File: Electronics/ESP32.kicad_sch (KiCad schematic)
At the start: 13 parts, among them Q10 RSC002P03, Q7 BSH108, Q8 BSH108, Q9 BSH108, U9 ESP32-WROOM-32D

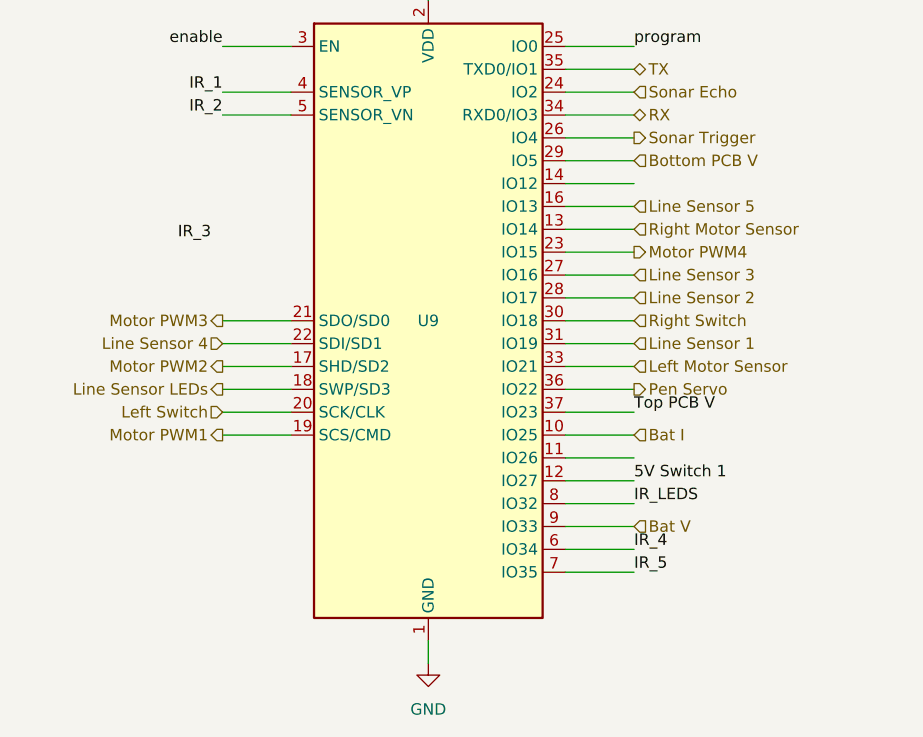
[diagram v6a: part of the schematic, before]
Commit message: Fixed the enable pin being used
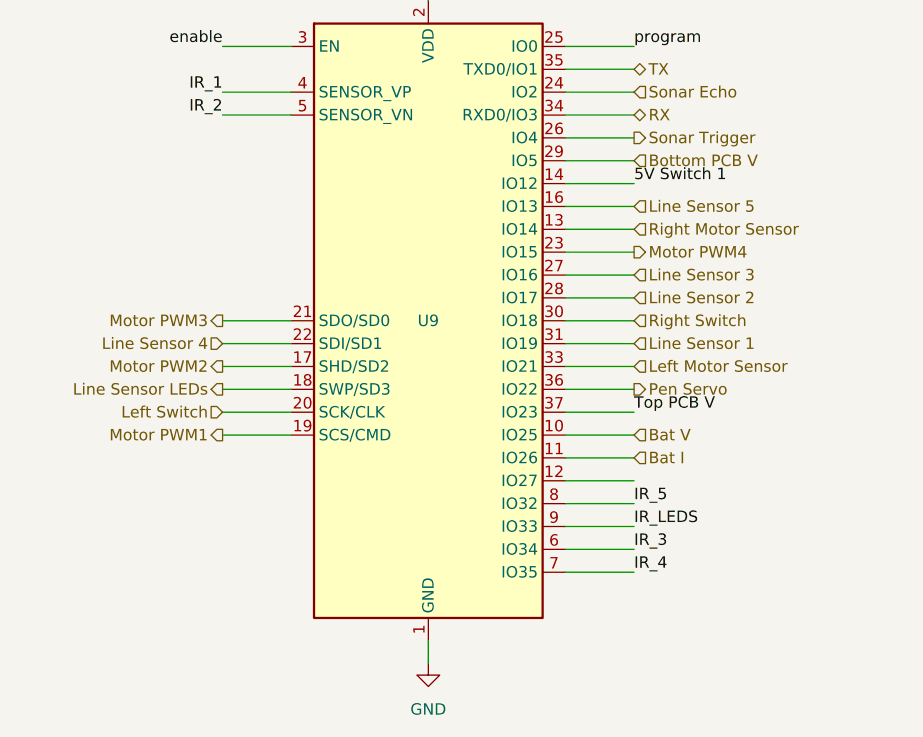
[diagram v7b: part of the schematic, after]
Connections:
- net 5V Switch 1: now also U9.14 (IO12); no longer U9.12 (IO27)
- net Bat I: now also U9.11 (IO26); no longer U9.10 (IO25)
- net Bat V: now also U9.10 (IO25); no longer U9.9 (IO33)
- net IR_3: now also U9.6 (IO34)
- net IR_4: now also U9.7 (IO35); no longer U9.6 (IO34)
- net IR_5: now also U9.8 (IO32); no longer U9.7 (IO35)
- net IR_LEDS: now also U9.9 (IO33); no longer U9.8 (IO32)
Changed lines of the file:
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@@
     (comment 1 "Design by Philip McGaw")
   )
-  (junction (at 64.77 121.92) (diameter 0) (color 0 0 0 0))
+  (junction (at 64.77 44.45) (diameter 0) (color 0 0 0 0))
   (junction (at 81.28 130.81) (diameter 0) (color 0 0 0 0))
   (junction (at 64.77 82.55) (diameter 0) (color 0 0 0 0))
   (junction (at 57.15 129.54) (diameter 0) (color 0 0 0 0))
   (junction (at 64.77 111.76) (diameter 0) (color 0 0 0 0))
-  (junction (at 64.77 44.45) (diameter 0) (color 0 0 0 0))
+  (junction (at 64.77 121.92) (diameter 0) (color 0 0 0 0))
   (wire (pts (xy 235.585 90.17) (xy 245.745 90.17))
     (stroke (width 0) (type default) (color 0 0 0 0))
@@
     (effects (font (size 1.27 1.27)) (justify left bottom))
   )
-  (label "IR_5" (at 182.88 102.87 0)
+  (label "IR_5" (at 182.88 95.25 0)
     (effects (font (size 1.27 1.27)) (justify left bottom))
   )
@@
     (effects (font (size 1.27 1.27)) (justify right bottom))
   )
-  (label "IR_4" (at 182.88 100.33 0)
+  (label "IR_4" (at 182.88 102.87 0)
     (effects (font (size 1.27 1.27)) (justify left bottom))
   )
@@
     (effects (font (size 1.27 1.27)) (justify right bottom))
   )
-  (label "5V Switch 1" (at 182.88 92.71 0)
+  (label "5V Switch 1" (at 182.88 59.69 0)
     (effects (font (size 1.27 1.27)) (justify left bottom))
   )
@@
     (effects (font (size 1.27 1.27)) (justify left bottom))
   )
-  (label "IR_LEDS" (at 182.88 95.25 0)
+  (label "IR_LEDS" (at 182.88 97.79 0)
     (effects (font (size 1.27 1.27)) (justify left bottom))
   )
@@
     (effects (font (size 1.27 1.27)) (justify right bottom))
   )
-  (label "IR_3" (at 135.89 66.04 180)
-    (effects (font (size 1.27 1.27)) (justify right bottom))
+  (label "IR_3" (at 182.88 100.33 0)
+    (effects (font (size 1.27 1.27)) (justify left bottom))
   )
   (label "IR_5" (at 235.585 102.87 180)
@@
     (effects (font (size 1.27 1.27)) (justify left))
   )
-  (hierarchical_label "Bat V" (shape input) (at 182.88 97.79 0)
+  (hierarchical_label "Bat V" (shape input) (at 182.88 87.63 0)
     (effects (font (size 1.27 1.27)) (justify left))
   )
@@
     (effects (font (size 1.27 1.27)) (justify right))
   )
-  (hierarchical_label "Bat I" (shape input) (at 182.88 87.63 0)
+  (hierarchical_label "Bat I" (shape input) (at 182.88 90.17 0)
     (effects (font (size 1.27 1.27)) (justify left))
   )
@@
   )
   (symbol (lib_id "power:+3V3") (at 236.22 36.83 0) (unit 1)
-    (in_bom yes) (on_board yes) (fields_autoplaced)
+    (in_bom yes) (on_board yes)
     (property "Reference" "#PWR035" (id 0) (at 236.22 40.64 0)
       (effects (font (size 1.27 1.27)) hide)

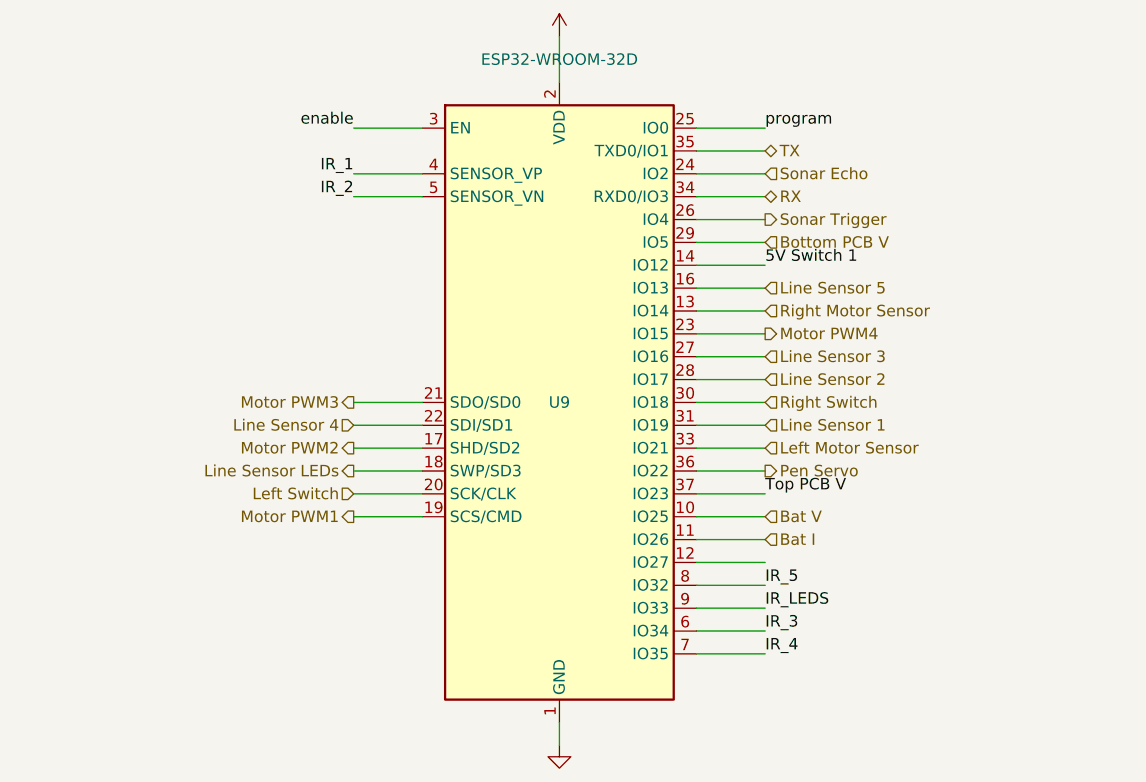
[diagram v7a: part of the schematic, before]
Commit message: Cleaning up the stupid error with the pinout
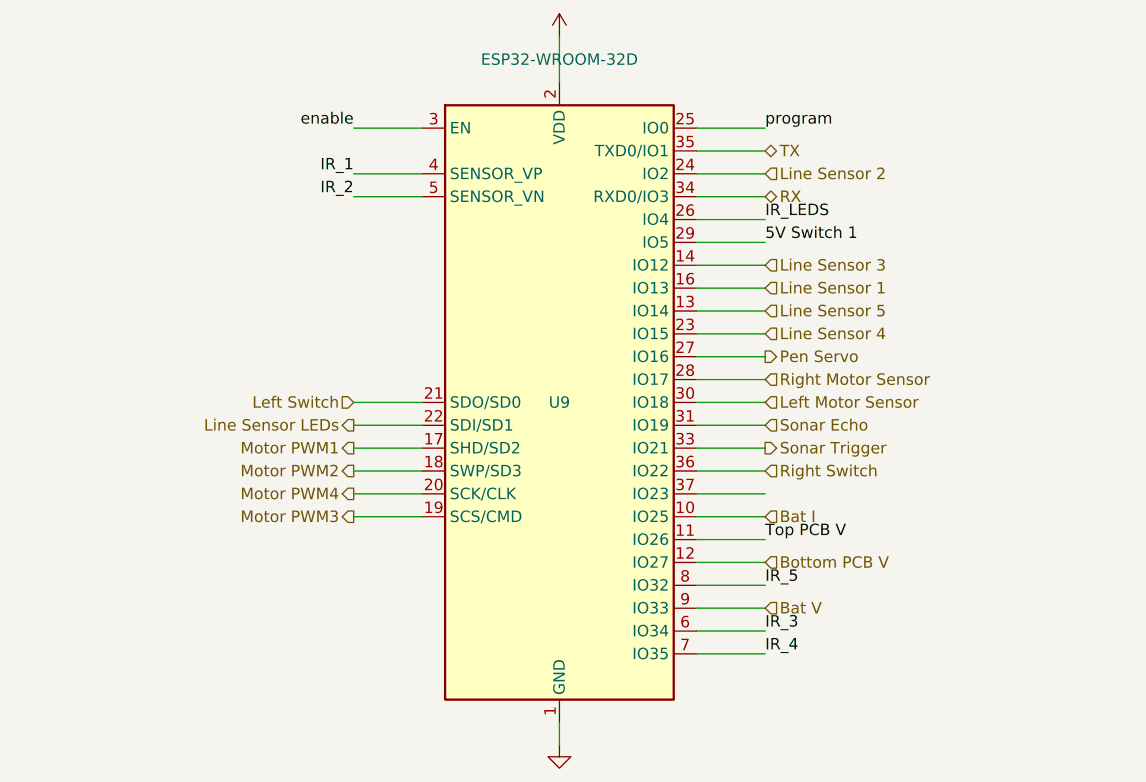
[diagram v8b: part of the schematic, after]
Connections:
- net 5V Switch 1: now also U9.29 (IO5); no longer U9.14 (IO12)
- net Bat I: now also U9.10 (IO25); no longer U9.11 (IO26)
- net Bat V: now also U9.9 (IO33); no longer U9.10 (IO25)
- net Bottom PCB V: now also U9.12 (IO27); no longer U9.29 (IO5)
- net IR_LEDS: now also U9.26 (IO4); no longer U9.9 (IO33)
- net Left Motor Sensor: now also U9.30 (IO18); no longer U9.33 (IO21)
- net Left Switch: now also U9.21 (SDO/SD0); no longer U9.20 (SCK/CLK)
- net Line Sensor 1: now also U9.16 (IO13); no longer U9.31 (IO19)
- net Line Sensor 2: now also U9.24 (IO2); no longer U9.28 (IO17)
- net Line Sensor 3: now also U9.14 (IO12); no longer U9.27 (IO16)
- net Line Sensor 4: now also U9.23 (IO15); no longer U9.22 (SDI/SD1)
- net Line Sensor 5: now also U9.13 (IO14); no longer U9.16 (IO13)
- net Line Sensor LEDs: now also U9.22 (SDI/SD1); no longer U9.18 (SWP/SD3)
- net Motor PWM1: now also U9.17 (SHD/SD2); no longer U9.19 (SCS/CMD)
- net Motor PWM2: now also U9.18 (SWP/SD3); no longer U9.17 (SHD/SD2)
- net Motor PWM3: now also U9.19 (SCS/CMD); no longer U9.21 (SDO/SD0)
- net Motor PWM4: now also U9.20 (SCK/CLK); no longer U9.23 (IO15)
- net Pen Servo: now also U9.27 (IO16); no longer U9.36 (IO22)
- net Right Motor Sensor: now also U9.28 (IO17); no longer U9.13 (IO14)
- net Right Switch: now also U9.36 (IO22); no longer U9.30 (IO18)
- net Sonar Echo: now also U9.31 (IO19); no longer U9.24 (IO2)
- net Sonar Trigger: now also U9.33 (IO21); no longer U9.26 (IO4)
- net Top PCB V: now also U9.11 (IO26); no longer U9.37 (IO23)
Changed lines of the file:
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@@
     (comment 1 "Design by Philip McGaw")
   )
+  (junction (at 64.77 111.76) (diameter 0) (color 0 0 0 0))
   (junction (at 64.77 44.45) (diameter 0) (color 0 0 0 0))
+  (junction (at 64.77 121.92) (diameter 0) (color 0 0 0 0))
+  (junction (at 57.15 129.54) (diameter 0) (color 0 0 0 0))
   (junction (at 81.28 130.81) (diameter 0) (color 0 0 0 0))
   (junction (at 64.77 82.55) (diameter 0) (color 0 0 0 0))
-  (junction (at 57.15 129.54) (diameter 0) (color 0 0 0 0))
-  (junction (at 64.77 111.76) (diameter 0) (color 0 0 0 0))
-  (junction (at 64.77 121.92) (diameter 0) (color 0 0 0 0))
   (wire (pts (xy 235.585 90.17) (xy 245.745 90.17))
     (stroke (width 0) (type default) (color 0 0 0 0))
@@
     (stroke (width 0) (type default) (color 0 0 0 0))
   )
+  (wire (pts (xy 55.88 120.65) (xy 57.15 120.65))
+    (stroke (width 0) (type default) (color 0 0 0 0))
+  )
   (wire (pts (xy 57.15 120.65) (xy 57.15 129.54))
-    (stroke (width 0) (type default) (color 0 0 0 0))
-  )
-  (wire (pts (xy 55.88 120.65) (xy 57.15 120.65))
     (stroke (width 0) (type default) (color 0 0 0 0))
   )
@@
     (effects (font (size 1.27 1.27)) (justify left bottom))
   )
-  (label "Top PCB V" (at 182.88 85.09 0)
+  (label "Top PCB V" (at 182.88 90.17 0)
     (effects (font (size 1.27 1.27)) (justify left bottom))
   )
@@
     (effects (font (size 1.27 1.27)) (justify right bottom))
   )
-  (label "5V Switch 1" (at 182.88 59.69 0)
+  (label "5V Switch 1" (at 182.88 57.15 0)
     (effects (font (size 1.27 1.27)) (justify left bottom))
   )
@@
     (effects (font (size 1.27 1.27)) (justify left bottom))
   )
-  (label "IR_LEDS" (at 182.88 97.79 0)
+  (label "IR_LEDS" (at 182.88 54.61 0)
     (effects (font (size 1.27 1.27)) (justify left bottom))
   )
@@
     (effects (font (size 1.27 1.27)) (justify left))
   )
-  (hierarchical_label "Motor PWM3" (shape output) (at 137.16 74.93 180)
-    (effects (font (size 1.27 1.27)) (justify right))
-  )
-  (hierarchical_label "Right Switch" (shape input) (at 182.88 74.93 0)
-    (effects (font (size 1.27 1.27)) (justify left))
-  )
-  (hierarchical_label "Left Motor Sensor" (shape input) (at 182.88 80.01 0)
+  (hierarchical_label "Motor PWM3" (shape output) (at 137.16 87.63 180)
+    (effects (font (size 1.27 1.27)) (justify right))
+  )
+  (hierarchical_label "Right Switch" (shape input) (at 182.88 82.55 0)
+    (effects (font (size 1.27 1.27)) (justify left))
+  )
+  (hierarchical_label "Left Motor Sensor" (shape input) (at 182.88 74.93 0)
     (effects (font (size 1.27 1.27)) (justify left))
   )
@@
     (effects (font (size 1.27 1.27)) (justify left))
   )
-  (hierarchical_label "Sonar Trigger" (shape output) (at 182.88 54.61 0)
-    (effects (font (size 1.27 1.27)) (justify left))
-  )
-  (hierarchical_label "Bat V" (shape input) (at 182.88 87.63 0)
-    (effects (font (size 1.27 1.27)) (justify left))
-  )
-  (hierarchical_label "Line Sensor 4" (shape input) (at 137.16 77.47 180)
-    (effects (font (size 1.27 1.27)) (justify right))
-  )
-  (hierarchical_label "Sonar Echo" (shape input) (at 182.88 49.53 0)
-    (effects (font (size 1.27 1.27)) (justify left))
-  )
-  (hierarchical_label "Right Motor Sensor" (shape input) (at 182.88 64.77 0)
-    (effects (font (size 1.27 1.27)) (justify left))
-  )
-  (hierarchical_label "Line Sensor 3" (shape input) (at 182.88 69.85 0)
+  (hierarchical_label "Sonar Trigger" (shape output) (at 182.88 80.01 0)
+    (effects (font (size 1.27 1.27)) (justify left))
+  )
+  (hierarchical_label "Bat V" (shape input) (at 182.88 97.79 0)
+    (effects (font (size 1.27 1.27)) (justify left))
+  )
+  (hierarchical_label "Line Sensor 4" (shape input) (at 182.88 67.31 0)
+    (effects (font (size 1.27 1.27)) (justify left))
+  )
+  (hierarchical_label "Sonar Echo" (shape input) (at 182.88 77.47 0)
+    (effects (font (size 1.27 1.27)) (justify left))
+  )
+  (hierarchical_label "Right Motor Sensor" (shape input) (at 182.88 72.39 0)
+    (effects (font (size 1.27 1.27)) (justify left))
+  )
+  (hierarchical_label "Line Sensor 3" (shape input) (at 182.88 59.69 0)
     (effects (font (size 1.27 1.27)) (justify left))
   )
@@
     (effects (font (size 1.27 1.27)) (justify right))
   )
-  (hierarchical_label "Line Sensor 5" (shape input) (at 182.88 62.23 0)
-    (effects (font (size 1.27 1.27)) (justify left))
-  )
-  (hierarchical_label "Motor PWM4" (shape output) (at 182.88 67.31 0)
-    (effects (font (size 1.27 1.27)) (justify left))
-  )
-  (hierarchical_label "Bottom PCB V" (shape input) (at 182.88 57.15 0)
-    (effects (font (size 1.27 1.27)) (justify left))
-  )
-  (hierarchical_label "Line Sensor 1" (shape input) (at 182.88 77.47 0)
-    (effects (font (size 1.27 1.27)) (justify left))
-  )
-  (hierarchical_label "Pen Servo" (shape output) (at 182.88 82.55 0)
-    (effects (font (size 1.27 1.27)) (justify left))
-  )
-  (hierarchical_label "Motor PWM2" (shape output) (at 137.16 80.01 180)
-    (effects (font (size 1.27 1.27)) (justify right))
-  )
-  (hierarchical_label "Bat I" (shape input) (at 182.88 90.17 0)
-    (effects (font (size 1.27 1.27)) (justify left))
-  )
-  (hierarchical_label "Line Sensor LEDs" (shape output) (at 137.16 82.55 180)
-    (effects (font (size 1.27 1.27)) (justify right))
-  )
-  (hierarchical_label "Line Sensor 2" (shape input) (at 182.88 72.39 0)
-    (effects (font (size 1.27 1.27)) (justify left))
-  )
-  (hierarchical_label "Motor PWM1" (shape output) (at 137.16 87.63 180)
-    (effects (font (size 1.27 1.27)) (justify right))
-  )
-  (hierarchical_label "Left Switch" (shape input) (at 137.16 85.09 180)
-    (effects (font (size 1.27 1.27)) (justify right))
-  )
+  (hierarchical_label "Line Sensor 5" (shape input) (at 182.88 64.77 0)
+    (effects (font (size 1.27 1.27)) (justify left))
+  )
+  (hierarchical_label "Motor PWM4" (shape output) (at 137.16 85.09 180)
+    (effects (font (size 1.27 1.27)) (justify right))
+  )
+  (hierarchical_label "Bottom PCB V" (shape input) (at 182.88 92.71 0)
+    (effects (font (size 1.27 1.27)) (justify left))
+  )
+  (hierarchical_label "Line Sensor 1" (shape input) (at 182.88 62.23 0)
+    (effects (font (size 1.27 1.27)) (justify left))
+  )
+  (hierarchical_label "Pen Servo" (shape output) (at 182.88 69.85 0)
+    (effects (font (size 1.27 1.27)) (justify left))
+  )
+  (hierarchical_label "Motor PWM2" (shape output) (at 137.16 82.55 180)
+    (effects (font (size 1.27 1.27)) (justify right))
+  )
+  (hierarchical_label "Bat I" (shape input) (at 182.88 87.63 0)
+    (effects (font (size 1.27 1.27)) (justify left))
+  )
+  (hierarchical_label "Line Sensor LEDs" (shape output) (at 137.16 77.47 180)
+    (effects (font (size 1.27 1.27)) (justify right))
+  )
+  (hierarchical_label "Line Sensor 2" (shape input) (at 182.88 49.53 0)
+    (effects (font (size 1.27 1.27)) (justify left))
+  )
+  (hierarchical_label "Motor PWM1" (shape output) (at 137.16 80.01 180)
+    (effects (font (size 1.27 1.27)) (justify right))
+  )
+  (hierarchical_label "Left Switch" (shape input) (at 137.16 74.93 180)
+    (effects (font (size 1.27 1.27)) (justify right))
+  )
